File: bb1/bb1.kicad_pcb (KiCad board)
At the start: 4 copper layers, 101 x 56 mm, 100 parts, among them CON1 SD_Card, J1 USB-MICRO-B-SHIELDED, P1 PWR+CAN, P10 SPI_DBG, P11 RX1, P12 RX2, P13 CAN_RX, P14 CAN_TX, P2 WIFI_DBG, P3 CONN_01X08, P4 USB_POWER, P5 NMEA_RX, P6 CORTEX_DEBUG, P7 NMEA_TX, P8 BATTERIES, P9 SHUNT, Q1 MMBT3904, SW1 RESET, SW2 PROGRAM, SW3 SW_PUSH, U1 TL2575, U10 MCP2562, U11 SN75C3222E, U12 INA219, U13 BMP280, U14 MPL3115A2, U2 WIFI_RGB, U3 ESP-13-WROOM-02, U4 N2K_RGB, U5 NMEA_RGB, U6 ILI9341_LCD_Breakout, U7 LP38691, U8 MK20DX256VLH7, U9 MKL02Z32VFG4, X1 CRYSTAL_SMD, Y2 32kHz

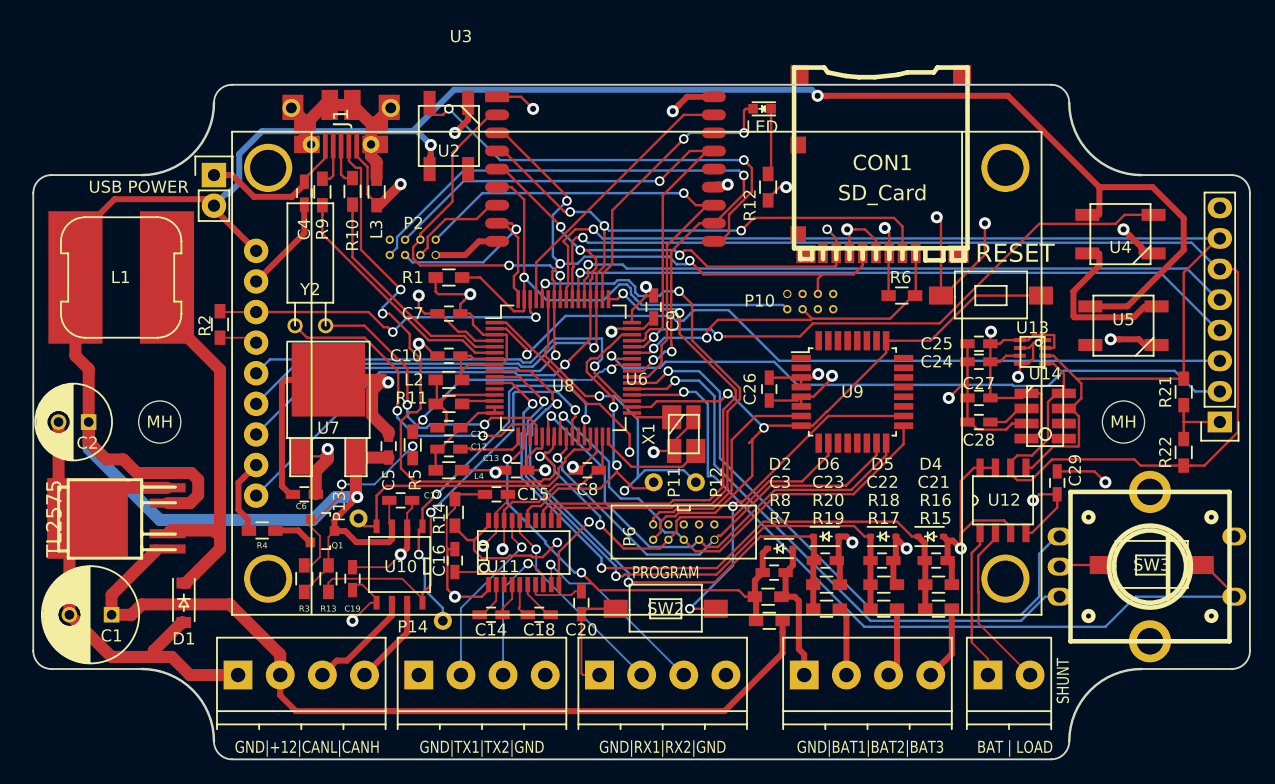
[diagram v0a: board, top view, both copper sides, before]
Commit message: Fine tuning of the board
- Added test headers for serial1, serial2 and can (at 3.3v levels)
- Added solder jumpers to disconnect serial2 from rs232 converter
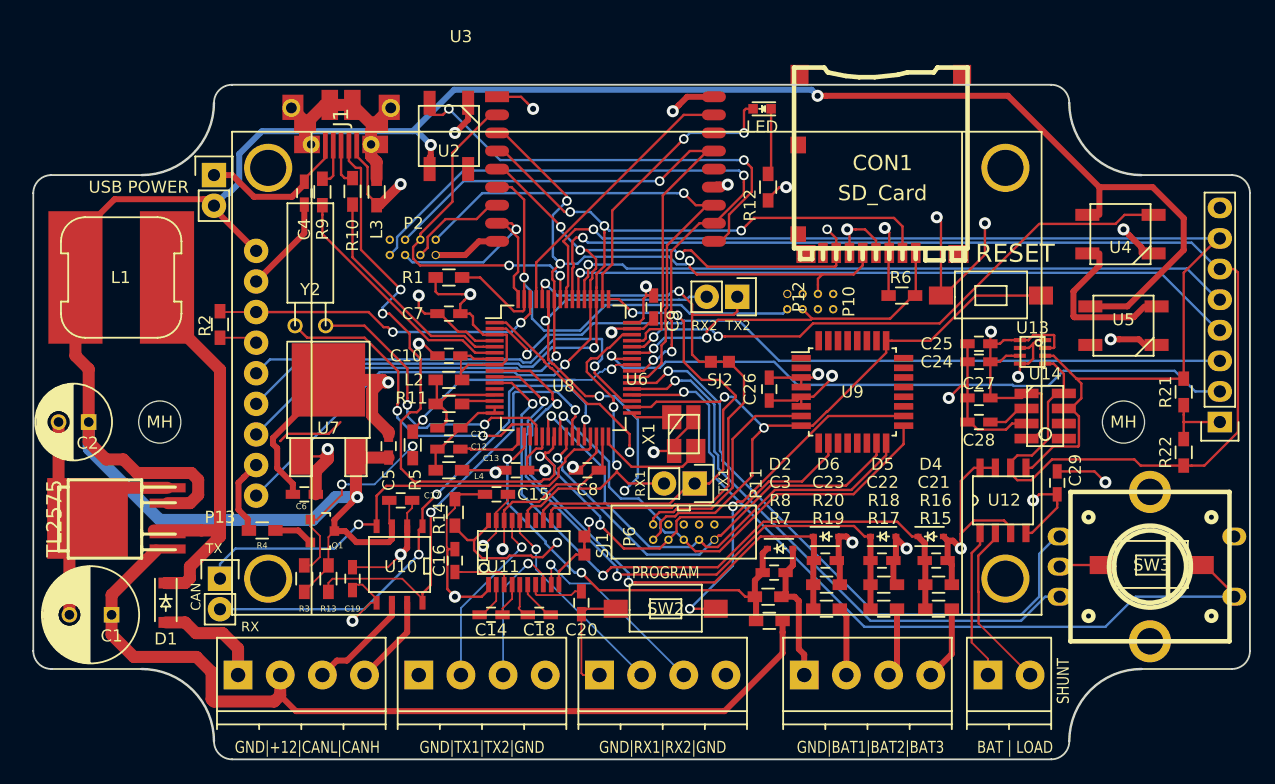
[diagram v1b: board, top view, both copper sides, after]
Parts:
- removed P14: CAN_TX, Measurement_Points:Measurement_Point_Round-TH_Small
- added SJ1: SOLDER_JUMPER, bb:SolderJumper, F.Cu at (82.2, 112.2)
- added SJ2: SOLDER_JUMPER, bb:SolderJumper, F.Cu at (93.5, 97.0)
- P11: value RX1 -> CONN_01X02; footprint Measurement_Points:Measurement_Point_Round-TH_Small -> Pin_Headers:Pin_Header_Straight_1x02
- P12: value RX2 -> CONN_01X02; footprint Measurement_Points:Measurement_Point_Round-TH_Small -> Pin_Headers:Pin_Header_Straight_1x02
- P13: value CAN_RX -> CONN_01X02; footprint Measurement_Points:Measurement_Point_Round-TH_Small -> Pin_Headers:Pin_Header_Straight_1x02
- moved P12 15.8 mm to (94.9, 91.6), turned to 270 degrees
- moved P13 12.5 mm to (52.0, 115.0)
- moved P11 3.40 mm to (91.4, 107.1), turned to 270 degrees
- moved D1 1.50 mm to (47.5, 117.0)
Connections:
- P11 pad 1: /Teensy/9 -> /Teensy/10
- P12 pad 1: /Teensy/7 -> /Teensy/8
- U11 pad 10: /Teensy/7 -> Net-(SJ1-Pad1)
- U11 pad 12: /Teensy/8 -> Net-(SJ2-Pad2)
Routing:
- net Net-(SJ2-Pad2): track 0.00 -> 27.7 mm
- net /Teensy/8: track 48.7 -> 26.2 mm
- net /Teensy/4: track 25.3 -> 39.1 mm, vias 0 -> 1
- net GND: track 283.1 -> 270.5 mm
- net /Teensy/3: track 32.9 -> 45.0 mm
- net (no net): track 0.00 -> 5.65 mm
- net /Teensy/7: track 36.8 -> 42.4 mm, vias 3 -> 4
- net Net-(SJ1-Pad1): track 0.00 -> 4.56 mm
- net Net-(D1-Pad1): track 33.0 -> 36.5 mm
- net /Teensy/21/A7: track 42.7 -> 44.8 mm
- net +12V: track 73.3 -> 75.0 mm
- net /Teensy/26: track 64.9 -> 63.9 mm
- net /Teensy/20/A6: track 29.1 -> 28.3 mm
- net /Teensy/A12: track 55.3 -> 56.1 mm
- net /Teensy/9: track 28.0 -> 28.7 mm
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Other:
- board text added: "CAN"
- board text added: "RX"
- board text added: "RX1"
- board text added: "RX2"
- board text added: "TX"
- board text added: "TX1"
- board text added: "TX2"

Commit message: Continued work on the PCB. Lots of footprint work.
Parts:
- removed the MH at (127.0, 102.0)
- removed the MH at (47.0, 102.0)
- removed SW2: PROGRAM, bb:SWITCH_SMD_3x6
- added G***: LOGO, bb:BLUECOCONUT-LOGO_45mm, B.Cu at (111.7, 98.5)
- added MH: MountingHole_4-5mm, Mounting_Holes:MountingHole_4-5mm, F.Cu at (47.0, 102.0)
- added REF**: Symbol_OSHW-Logo_SilkScreen_BIG, Symbols:Symbol_OSHW-Logo_SilkScreen_BIG, B.Cu at (69.8, 77.5)
- added REF**: MountingHole_4-5mm, Mounting_Holes:MountingHole_4-5mm, F.Cu at (127.0, 102.0)
- added SJ3: SOLDER_JUMPER, bb:SolderJumper, F.Cu at (97.5, 104.5)
- CON1: value SD_Card -> MICROSD; footprint w_conn_misc:microsd_socket -> bb:DM3CS-SF
- SW1: value RESET -> PROGRAM
- U1: value TL2575 -> U1
- U10: footprint SMD_Packages:SOIC-8-N -> gsg-modules:SOIC8-208
- U11: footprint SMD_Packages:SSOP-20 -> bb:SSOP-20-HandSoldering
- U12: footprint bb:INA219 -> gsg-modules:SOIC8-208
- Y2: footprint Crystals:Crystal_Watch -> bb:Crystal_Watch_6mm
- moved SW1 37.5 mm to (89.0, 117.5)
- moved R6 10.7 mm to (117.1, 85.0), turned to 180 degrees
- moved R21 7.57 mm to (133.0, 107.0), turned to 180 degrees
- moved C2 4.08 mm to (39.0, 98.5), turned to 270 degrees
- moved C29 3.65 mm to (125.0, 106.0), turned to 0 degrees
- moved C15 3.39 mm to (71.6, 108.5)
- moved C16 2.55 mm to (71.0, 116.0), turned to 270 degrees
- moved R14 2.45 mm to (71.0, 111.9)
- moved L3 1.50 mm to (66.5, 83.0)
- moved CON1 1.37 mm to (107.2, 81.9)
- moved U12 1.17 mm to (116.7, 107.4), turned to 180 degrees
- moved P3 1.12 mm to (134.0, 101.5)
- moved R22 1.11 mm to (133.0, 105.0), turned to 180 degrees
- moved SW3 1.05 mm to (128.5, 114.5)
- moved E1 0.86 mm to (128.5, 114.5)
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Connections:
- CON1 pad 1: /Teensy/15/A1 -> Net-(CON1-Pad1)
- CON1 pad 2: /Teensy/11 -> /Teensy/15/A1
- CON1 pad 3: +3V3 -> /Teensy/11
- CON1 pad 4: GND -> +3V3
- P3 pad 1: +3V3 -> GND
- P3 pad 8: GND -> +3V3
- SJ1 pad 1: Net-(SJ1-Pad1) -> /Teensy/7
- SJ2 pad 2: Net-(SJ2-Pad2) -> /Teensy/8
- SW1 pad 1: /Teensy/RESET -> Net-(SJ3-Pad1)
- U11 pad 10: Net-(SJ1-Pad1) -> /Teensy/7
- U11 pad 12: Net-(SJ2-Pad2) -> /Teensy/8
- U9 pad 18: Net-(SW2-Pad1) -> Net-(SJ3-Pad1)
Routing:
- net Net-(SJ3-Pad1): track 0.00 -> 30.7 mm, vias 0 -> 2
- net /Teensy/8: track 26.2 -> 55.7 mm
- net Net-(SW2-Pad1): track 29.4 -> 0.00 mm, vias 2 -> 0
- net Net-(SJ2-Pad2): track 27.7 -> 0.00 mm
- net /Teensy/15/A1: track 30.9 -> 57.0 mm
- net GND: track 270.5 -> 246.2 mm
- net /Teensy/30: track 98.2 -> 121.4 mm
- net +5V: track 209.4 -> 231.7 mm, vias 3 -> 5
- net /Teensy/14/A0: track 79.9 -> 93.8 mm
- net /Teensy/12: track 83.4 -> 96.6 mm
- net /Teensy/RESET: track 55.8 -> 42.9 mm
- net /Teensy/29: track 109.0 -> 120.9 mm, vias 1 -> 3
- net Net-(P9-Pad2): track 14.2 -> 24.3 mm
- net /Teensy/7: track 42.4 -> 48.9 mm
- net (no net): track 5.65 -> 0.00 mm
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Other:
- board size 101 x 56 mm -> 100 x 56 mm
- board text added: "25"
- board text added: "26"
- board text added: "27"
- board text added: "28"
- board text added: "3.3V"
- board text added: "Blue Nexus v0.1 Copyright Thomas Sarlandie - 2015"
- board text added: "GND"
- board text added: "SCL"
- board text added: "SDA"
- board text removed: "BB1 v0.1 Open Source Hardware Copyright Thomas Sarlandie - 2015"
- board text removed: "RESET"

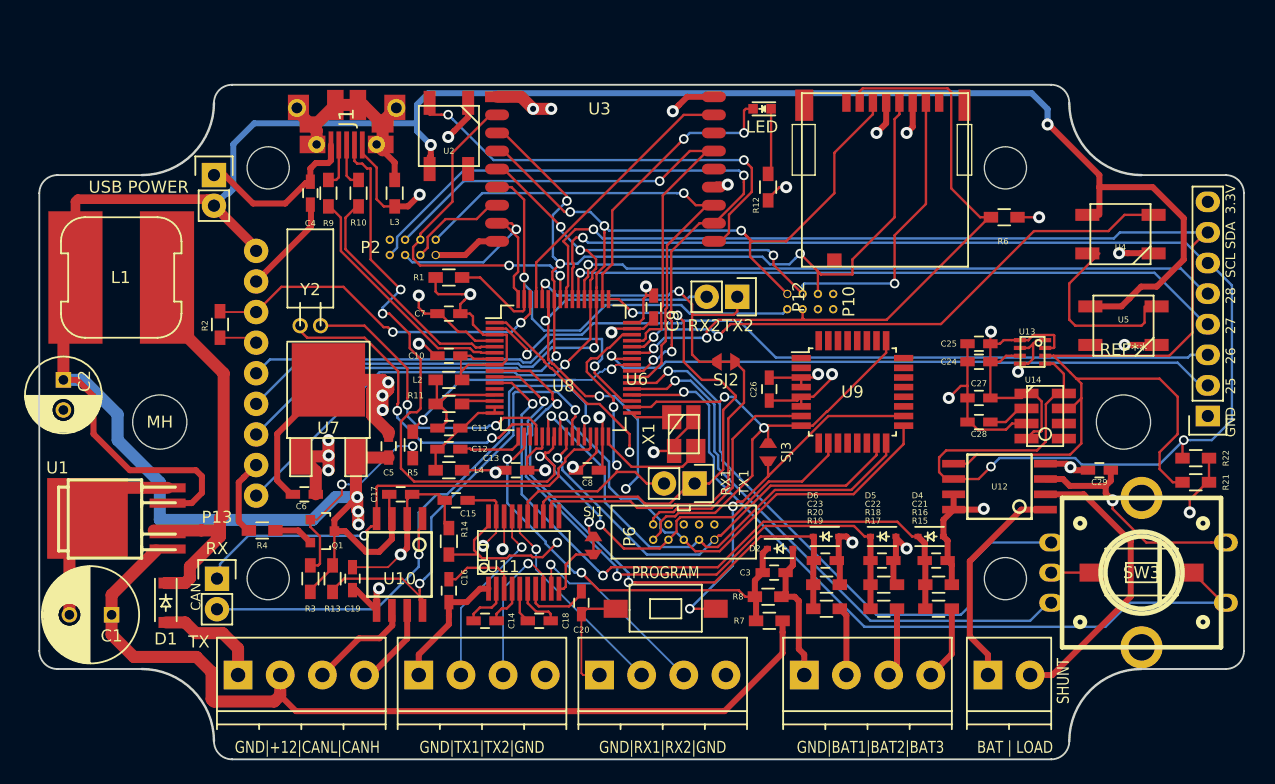
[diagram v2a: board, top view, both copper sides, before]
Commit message: Finalized v1 revA
 - Added BNO055
 - Fixed SOIC8 pattern
 - Replaced phoenix connectors by a 20 pol
 - Many fine tuning/cosmetic adjustments
 - Sent files to manufacturing. Will tag this commit.
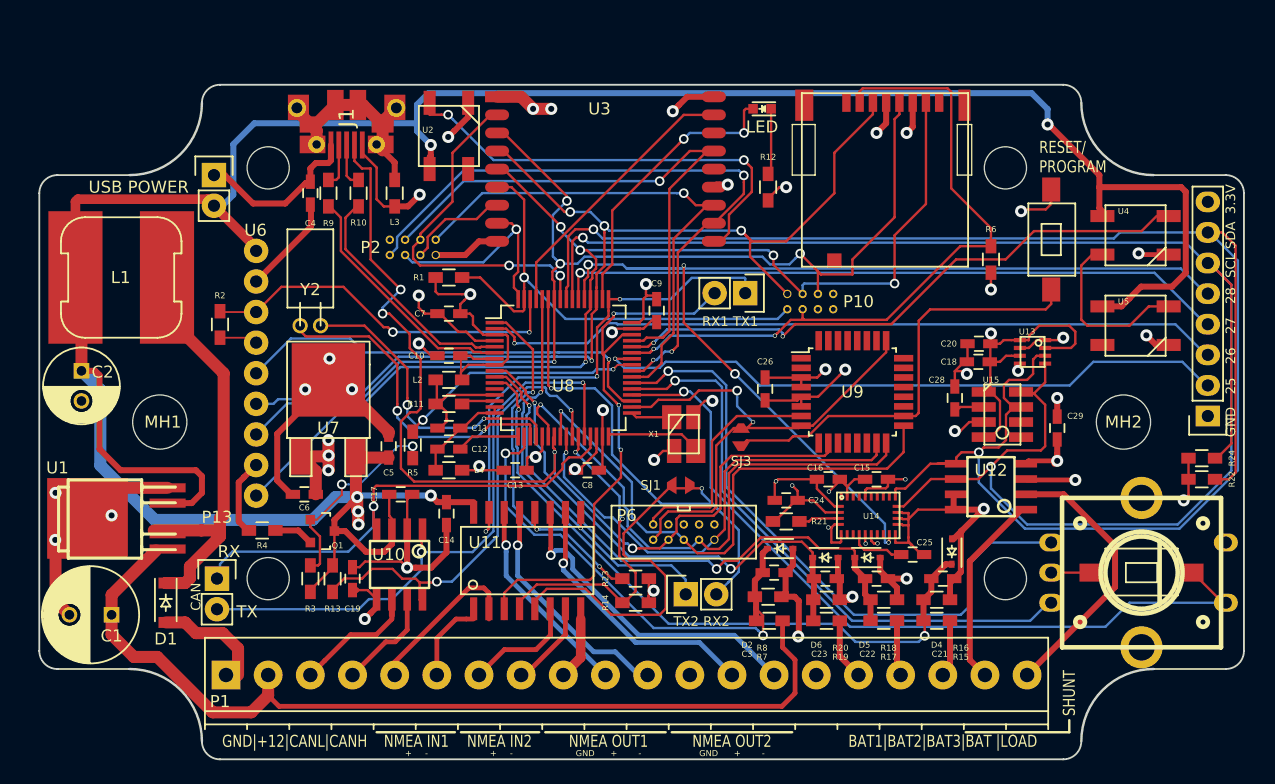
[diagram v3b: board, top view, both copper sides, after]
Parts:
- removed C27: .1uF, Capacitors_SMD:C_0603_HandSoldering
- removed MH, REF**: MountingHole_4-5mm, Mounting_Holes:MountingHole_4-5mm
- removed P5: NMEA_RX, Terminal_Blocks:TerminalBlock_Pheonix_PT-3.5mm_4pol
- removed P7: NMEA_TX, Terminal_Blocks:TerminalBlock_Pheonix_PT-3.5mm_4pol
- removed P8: BATTERIES, Terminal_Blocks:TerminalBlock_Pheonix_PT-3.5mm_4pol
- removed P9: SHUNT, Terminal_Blocks:TerminalBlock_Pheonix_PT-3.5mm_2pol
- removed REF**: Symbol_OSHW-Logo_SilkScreen_BIG, Symbols:Symbol_OSHW-Logo_SilkScreen_BIG
- removed SJ2: SOLDER_JUMPER, bb:SolderJumper
- added MH1: MOUNTING-HOLE, Mounting_Holes:MountingHole_4-5mm, F.Cu at (47.0, 102.0)
- added MH2: MOUNTING-HOLE, Mounting_Holes:MountingHole_4-5mm, F.Cu at (127.0, 102.0)
- added R23: 10k, Resistors_SMD:R_0603_HandSoldering, F.Cu at (86.5, 115.0)
- added R24: 4.7k, Resistors_SMD:R_0603_HandSoldering, F.Cu at (133.5, 105.0)
- added U15: MPL3115A2, bb:MPL3115A2, F.Cu at (117.0, 101.4)
- C15: value .1uF -> 6.8nF
- C16: value .1uF -> 120nF
- P1: value PWR+CAN -> CONN_01X20; footprint Terminal_Blocks:TerminalBlock_Pheonix_PT-3.5mm_4pol -> bb:TerminalBlock_Pheonix_PT-3.5mm_20pol
- R21: value 4.7k -> 10k
- U10, U12: footprint gsg-modules:SOIC8-208 -> bb:SOIC8N-HandSoldering
- U11: value SN75C3222E -> SN7534051; footprint bb:SSOP-20-HandSoldering -> bb:SOIC-16_5.6x10.5mm_Pitch1.27mm-HandSolder
- U14: value MPL3115A2 -> BNO055; footprint bb:MPL3115A2 -> bb:BNO055
- moved SW1 44.3 mm to (121.0, 86.8), turned to 270 degrees
- moved C18 42.3 mm to (115.0, 97.0), turned to 180 degrees
- moved C20 39.4 mm to (115.0, 95.5), turned to 180 degrees
- moved C15 34.9 mm to (106.5, 106.8)
- moved R21 34.2 mm to (99.0, 110.2), turned to 0 degrees
- moved C16 32.8 mm to (102.5, 106.8), turned to 0 degrees
- moved P12 25.1 mm to (90.7, 116.3), turned to 90 degrees
- moved C24 19.7 mm to (99.0, 108.5)
- moved C25 18.3 mm to (109.5, 113.0), turned to 0 degrees
- moved U14 16.8 mm to (105.8, 109.8)
- moved P11 16.3 mm to (95.6, 91.3)
- moved R14 16.3 mm to (86.5, 117.0), turned to 0 degrees
- moved C14 9.46 mm to (70.8, 109.6), turned to 270 degrees
- moved SJ1 8.81 mm to (90.2, 107.2), turned to 0 degrees
- moved C29 4.95 mm to (121.5, 102.5), turned to 90 degrees
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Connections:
- net Net-(P1-Pad3) renamed /NMEA/CAN-
- net Net-(P1-Pad4) renamed /NMEA/CAN+
- C14 pad 1: Net-(C14-Pad1) -> +5V
- C14 pad 2: Net-(C14-Pad2) -> GND
- C15 pad 1: +3V3 -> GND
- C15 pad 2: GND -> +3V3
- C16 pad 1: Net-(C16-Pad1) -> GND
- C16 pad 2: GND -> +3V3
- C18 pad 1: Net-(C18-Pad1) -> +3V3
- C18 pad 2: Net-(C18-Pad2) -> GND
- C20 pad 1: Net-(C20-Pad1) -> +3V3
- C25 pad 1: +3V3 -> Net-(C25-Pad1)
- R14 pad 1: GND -> /Teensy/24
- R14 pad 2: /Teensy/31 -> GND
- R15 pad 2: Net-(P8-Pad4) -> /NMEA/12V_3
- R17 pad 2: Net-(P8-Pad3) -> /NMEA/12V_2
- R19 pad 2: Net-(P8-Pad2) -> /NMEA/12V_1
- R21 pad 2: /Teensy/30 -> Net-(R21-Pad2)
- R22 pad 2: /Teensy/29 -> /Teensy/30
- U11 pad 1: GND -> /NMEA/NMEA_IN1-
- U11 pad 10: /Teensy/7 -> /NMEA/NMEA_OUT2+
- U11 pad 11: Net-(U11-Pad11) -> /NMEA/NMEA_OUT2-
- U11 pad 12: /Teensy/8 -> /Teensy/31
- U11 pad 13: /Teensy/10 -> /NMEA/NMEA_OUT1-
- U11 pad 14: Net-(U11-Pad14) -> /NMEA/NMEA_OUT1+
- U11 pad 15: /Teensy/9 -> /Teensy/10
- U11 pad 16: /NMEA/NMEA1_RX -> +5V
- U11 pad 2: Net-(C14-Pad1) -> /NMEA/NMEA_IN1+
- U11 pad 3: Net-(C16-Pad1) -> /Teensy/9
- U11 pad 4: Net-(C14-Pad2) -> /Teensy/24
- U11 pad 5: Net-(C18-Pad1) -> /Teensy/7
- U11 pad 6: Net-(C18-Pad2) -> /NMEA/NMEA_IN2+
- U11 pad 7: Net-(C20-Pad1) -> /NMEA/NMEA_IN2-
- U11 pad 8: /NMEA/NMEA2_TX -> GND
- U11 pad 9: /NMEA/NMEA2_RX -> /Teensy/8
- U12 pad 1: Net-(P9-Pad1) -> /NMEA/SHUNT+
- U12 pad 2: Net-(P9-Pad2) -> /NMEA/SHUNT-
- U14 pad 1: +3V3 -> Net-(U14-Pad1)
- U14 pad 2: Net-(C28-Pad1) -> GND
- U14 pad 3: GND -> +3V3
- U14 pad 4: +3V3 -> Net-(R21-Pad2)
- U14 pad 5: Net-(U14-Pad5) -> GND
- U14 pad 6: Net-(U14-Pad6) -> GND
- U14 pad 7: /Teensy/30 -> Net-(U14-Pad7)
- U14 pad 8: /Teensy/29 -> Net-(U14-Pad8)
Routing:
- net /Teensy/28: track 55.4 -> 91.2 mm, vias 1 -> 4
- net /Teensy/30: track 121.4 -> 153.9 mm, vias 1 -> 2
- net /Teensy/24: track 0.00 -> 27.9 mm, vias 0 -> 2
- net /NMEA/NMEA_OUT2-: track 0.00 -> 27.9 mm, vias 0 -> 1
- net Net-(P9-Pad2): track 24.3 -> 0.00 mm
- net /Teensy/29: track 120.9 -> 144.1 mm, vias 3 -> 2
- net /NMEA/NMEA_OUT2+: track 0.00 -> 23.0 mm, vias 0 -> 1
- net /NMEA/SHUNT-: track 0.00 -> 22.9 mm
- net /Teensy/7: track 48.9 -> 69.6 mm, vias 4 -> 2
- net /Teensy/8: track 55.7 -> 35.9 mm
- net /NMEA/NMEA_OUT1-: track 0.00 -> 19.5 mm, vias 0 -> 1
- net Net-(P9-Pad1): track 18.1 -> 0.00 mm
- net /Teensy/9: track 28.8 -> 46.1 mm, vias 2 -> 3
- net /NMEA/NMEA1_RX: track 17.0 -> 0.00 mm, vias 1 -> 0
- net /NMEA/NMEA_OUT1+: track 0.00 -> 17.0 mm, vias 0 -> 1
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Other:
- outline, holes or cut-outs redrawn
- net class 12V: clearance 0.5 -> 0.3
- rule pad_to_mask_clearance: 0.2 -> 0.0762
- rule trace_min: 0.1524 -> 0.127
- rule via_min_drill: 0.3302 -> 0.254
- rule via_min_size: 0.6858 -> 0.3556
- board text added: "+ -"
- board text added: "BAT1|BAT2|BAT3|BAT |LOAD"
- board text added: "Blue Nexus v1 revA Copyright Thomas Sarlandie - 2015"
- board text added: "GND + -"
- board text added: "NMEA IN1"
- board text added: "NMEA IN2"
- board text added: "NMEA OUT1"
- board text added: "NMEA OUT2"
- board text added: "RESET/ PROGRAM"
- board text added: "RX1 TX1"
- board text added: "TX2 RX2"
- board text removed: "BAT | LOAD"
- board text removed: "Blue Nexus v0.1 Copyright Thomas Sarlandie - 2015"
- board text removed: "GND|BAT1|BAT2|BAT3"
- board text removed: "GND|RX1|RX2|GND"
- board text removed: "GND|TX1|TX2|GND"
- board text removed: "PROGRAM"
- board text removed: "RX1"
- board text removed: "RX2"
- board text removed: "TX1"
- board text removed: "TX2"
